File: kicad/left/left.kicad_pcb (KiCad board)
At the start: 2 copper layers, 126 x 47.8 mm, 33 parts, among them J1 59453-121110ECHLF, J2 59453-051110ECHLF, J5 59453-081110EDHLF, U1 RP2040_Zero

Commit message: Add connectors
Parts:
- added J3: Conn_01x06_Pin, footprints:Pointing-connector, F.Cu at (71.5, 85.0)
- added J4: Conn_01x05_Pin, footprints:Joystick-connector, F.Cu at (124.8, 91.5)
- moved J1 18.5 mm to (75.0, 90.2)
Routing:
- net 3V3: track 83.2 -> 107.4 mm, vias 4 -> 3
- net MOSI: track 63.8 -> 85.4 mm, vias 2 -> 1
- net SS: track 61.1 -> 80.8 mm, vias 2 -> 1
- net MISO: track 61.9 -> 78.6 mm, vias 2 -> 3
- net SCK: track 64.4 -> 78.2 mm, vias 2 -> 1
- net GND: track 7.98 -> 15.7 mm, vias 2 -> 0
- net Col 2: track 94.6 -> 90.4 mm, vias 4 -> 5
- net Col 1: track 126.3 -> 124.1 mm, vias 4 -> 2
- net Row 4: track 139.0 -> 137.5 mm
- net Col 3: track 65.0 -> 63.9 mm
- net Col 4: track 28.0 -> 28.9 mm
- net Row 5: track 139.6 -> 138.9 mm
- net JC: track 29.0 -> 28.9 mm, vias 1 -> 0
- net JX: track 26.4 -> 26.3 mm, vias 2 -> 1
- net JY: vias 2 -> 1

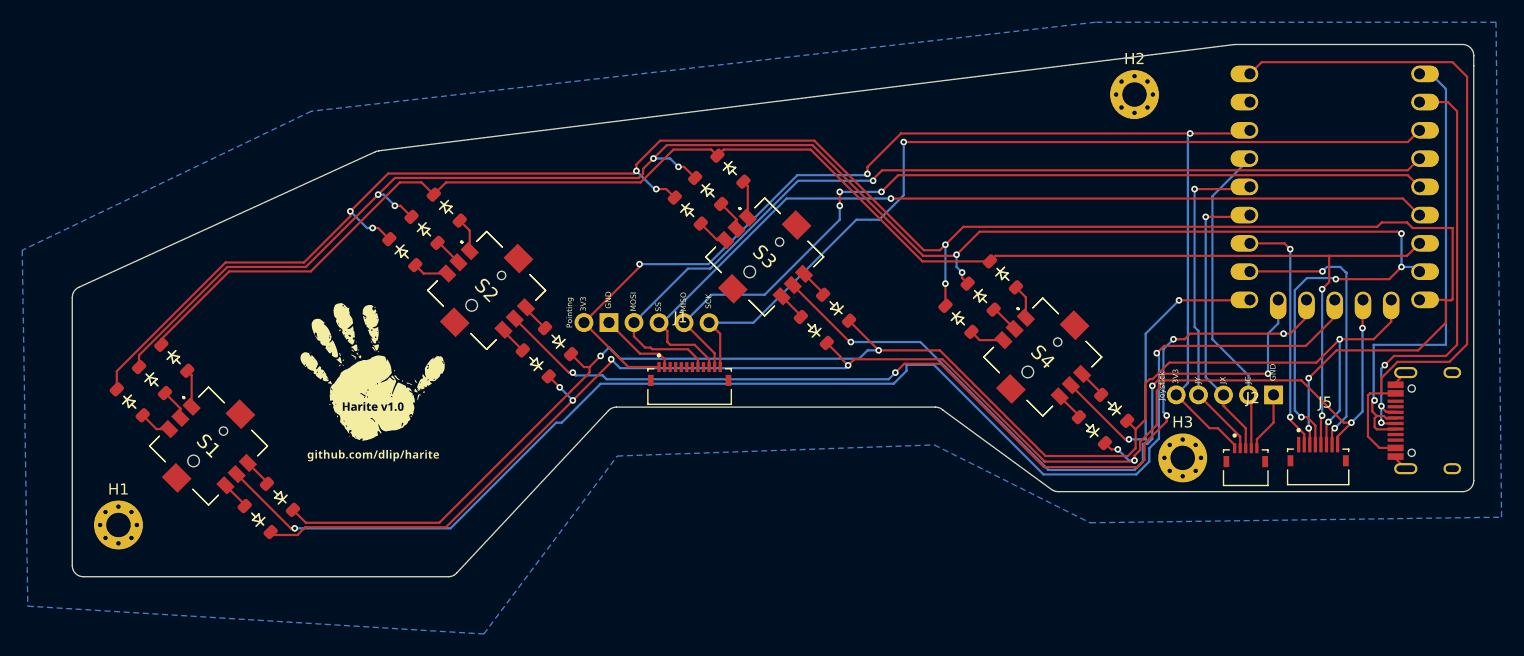
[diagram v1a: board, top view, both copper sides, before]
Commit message: Update footprints
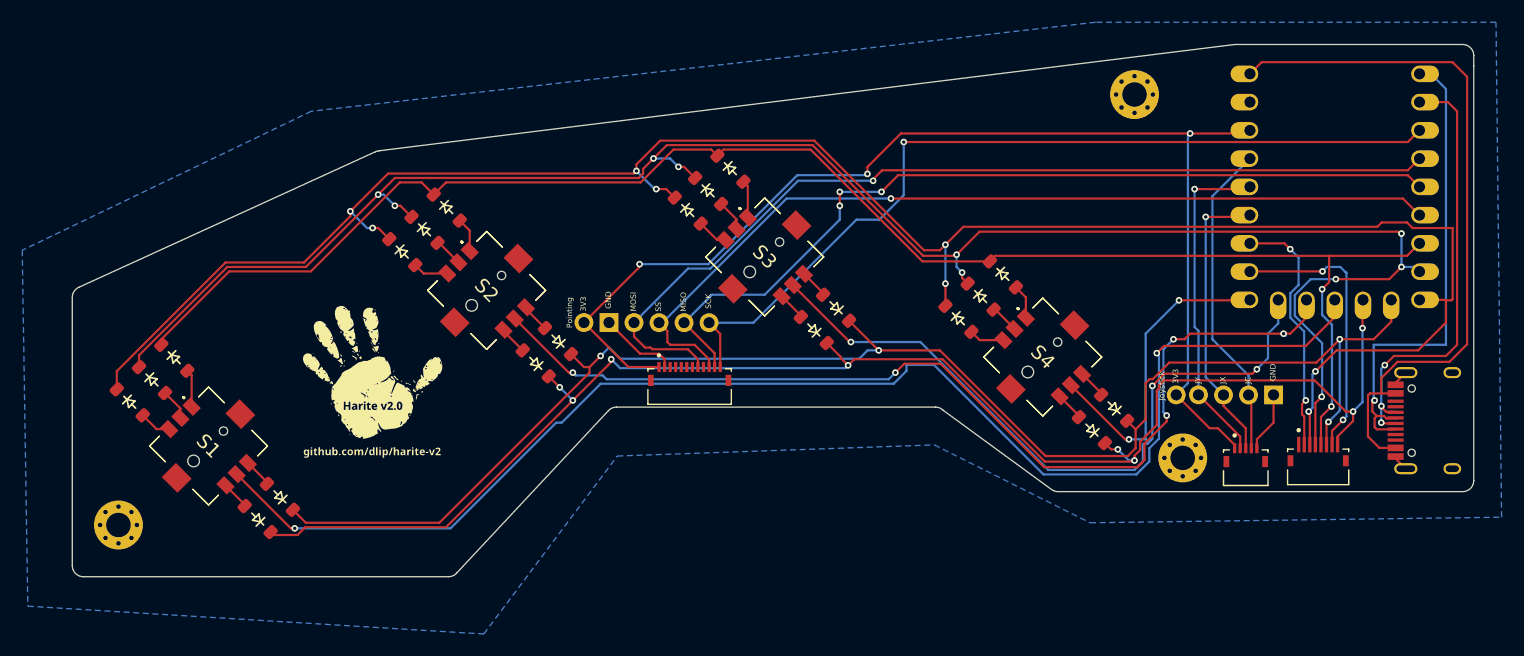
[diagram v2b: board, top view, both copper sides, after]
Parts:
- H1, H2, H3: footprint MountingHole:MountingHole_2.2mm_M2_Pad_Via -> footprints:MountingHole_2.2mm_M2_Pad_Via
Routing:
- net Col 6: track 22.1 -> 23.0 mm
- net Col 3: track 63.9 -> 63.1 mm
- net Row 1: track 144.2 -> 144.9 mm
